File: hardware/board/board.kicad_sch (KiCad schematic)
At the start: 10 parts, among them J101 UART, J102 CM4_DEBUG, J103 DEBUG_PORT, U101 Oled

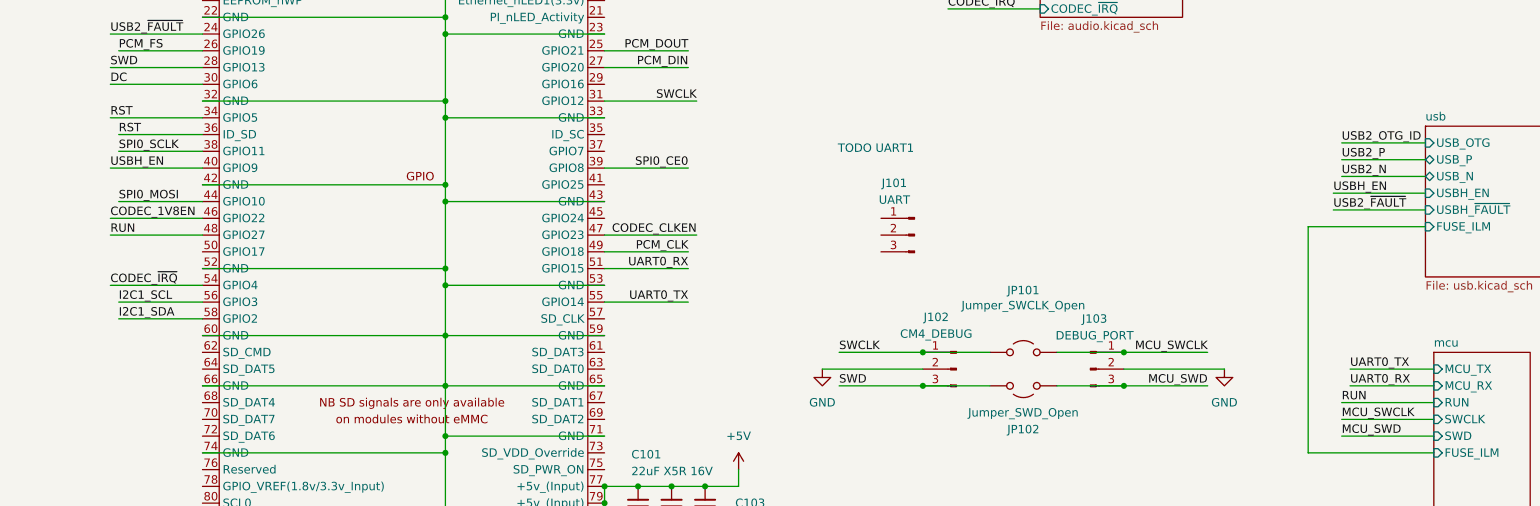
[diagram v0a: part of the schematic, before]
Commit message: wire encoder sw 3/4 and some cleanup
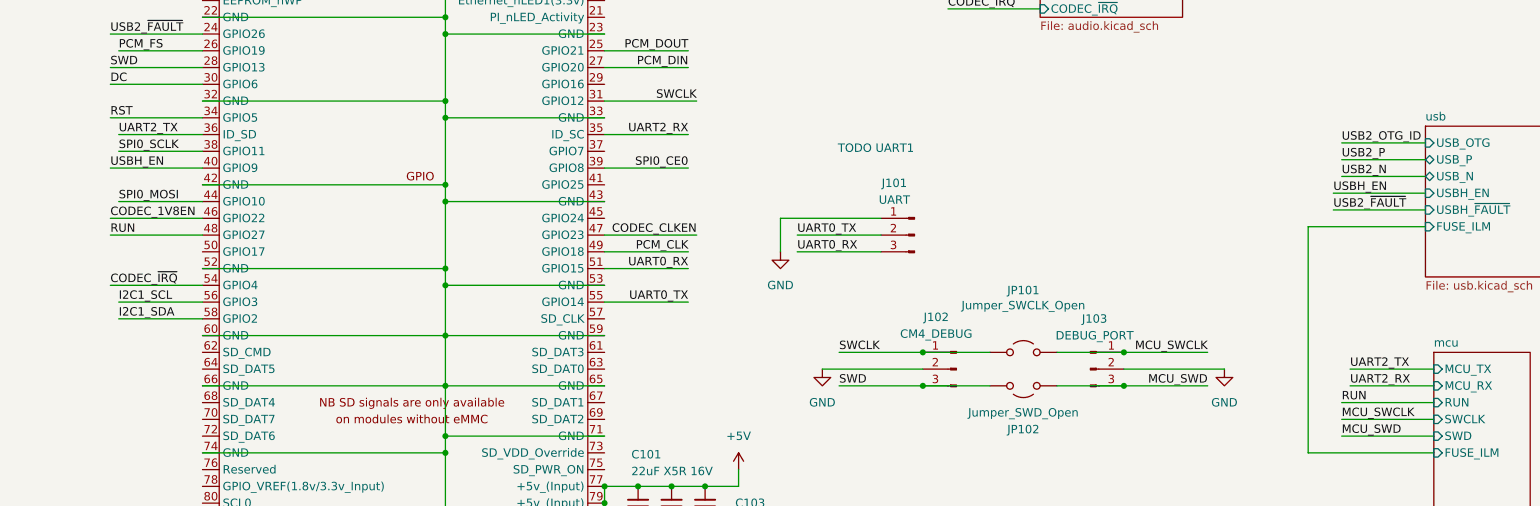
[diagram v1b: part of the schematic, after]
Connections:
- net GND: now also J101.1 (Pin_1)
- net RST: no longer Module101.36 (ID_SD)
- net UART0_RX: now also J101.3 (Pin_3)
- net UART0_TX: now also J101.2 (Pin_2)
- net UART2_RX: now reaches Module101.35 (ID_SC)
- new net UART2_TX: Module101.36 (ID_SD)
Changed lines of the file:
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@@
+	(wire
+		(pts
+			(xy 240.03 102.87) (xy 240.03 107.95)
+		)
+		(stroke
+			(width 0)
+			(type default)
+		)
+	)
 	(wire
 		(pts
@@
 	(wire
 		(pts
+			(xy 242.57 105.41) (xy 255.27 105.41)
+		)
+		(stroke
+			(width 0)
+			(type default)
+		)
+	)
+	(wire
+		(pts
 			(xy 261.62 128.27) (xy 271.78 128.27)
 		)
@@
 	(wire
 		(pts
+			(xy 242.57 107.95) (xy 255.27 107.95)
+		)
+		(stroke
+			(width 0)
+			(type default)
+		)
+	)
+	(wire
+		(pts
+			(xy 31.75 86.36) (xy 31.75 93.98)
+		)
+		(stroke
+			(width 0)
+			(type default)
+		)
+	)
+	(wire
+		(pts
+			(xy 138.43 74.93) (xy 152.4 74.93)
+		)
+		(stroke
+			(width 0)
+			(type default)
+		)
+	)
+	(wire
+		(pts
+			(xy 189.23 110.49) (xy 189.23 113.03)
+		)
+		(stroke
+			(width 0)
+			(type default)
+		)
+	)
+	(wire
+		(pts
+			(xy 255.27 102.87) (xy 240.03 102.87)
+		)
+		(stroke
+			(width 0)
+			(type default)
+		)
+	)
+	(wire
+		(pts
+			(xy 99.06 93.98) (xy 106.045 93.98)
+		)
+		(stroke
+			(width 0)
+			(type default)
+		)
+	)
+	(wire
+		(pts
+			(xy 189.23 54.61) (xy 189.23 62.23)
+		)
+		(stroke
+			(width 0)
+			(type default)
+		)
+	)
+	(wire
+		(pts
+			(xy 189.23 120.65) (xy 213.36 120.65)
+		)
+		(stroke
+			(width 0)
+			(type default)
+		)
+	)
+	(wire
+		(pts
+			(xy 31.75 139.7) (xy 31.75 147.32)
+		)
+		(stroke
+			(width 0)
+			(type default)
+		)
+	)
+	(wire
+		(pts
+			(xy 31.75 124.46) (xy 31.75 132.08)
+		)
+		(stroke
+			(width 0)
+			(type default)
+		)
+	)
+	(wire
+		(pts
+			(xy 106.045 78.74) (xy 106.045 86.36)
+		)
+		(stroke
+			(width 0)
+			(type default)
+		)
+	)
+	(wire
+		(pts
+			(xy 138.43 105.41) (xy 152.4 105.41)
+		)
+		(stroke
+			(width 0)
+			(type default)
+		)
+	)
+	(wire
+		(pts
 			(xy 326.39 125.73) (xy 339.09 125.73)
 		)
@@
 	(wire
 		(pts
-			(xy 31.75 86.36) (xy 31.75 93.98)
-		)
-		(stroke
-			(width 0)
-			(type default)
-		)
-	)
-	(wire
-		(pts
-			(xy 138.43 74.93) (xy 152.4 74.93)
-		)
-		(stroke
-			(width 0)
-			(type default)
-		)
-	)
-	(wire
-		(pts
-			(xy 189.23 110.49) (xy 189.23 113.03)
-		)
-		(stroke
-			(width 0)
-			(type default)
-		)
-	)
-	(wire
-		(pts
-			(xy 99.06 93.98) (xy 106.045 93.98)
-		)
-		(stroke
-			(width 0)
-			(type default)
-		)
-	)
-	(wire
-		(pts
-			(xy 189.23 54.61) (xy 189.23 62.23)
-		)
-		(stroke
-			(width 0)
-			(type default)
-		)
-	)
-	(wire
-		(pts
-			(xy 189.23 120.65) (xy 213.36 120.65)
-		)
-		(stroke
-			(width 0)
-			(type default)
-		)
-	)
-	(wire
-		(pts
-			(xy 31.75 139.7) (xy 31.75 147.32)
-		)
-		(stroke
-			(width 0)
-			(type default)
-		)
-	)
-	(wire
-		(pts
-			(xy 31.75 124.46) (xy 31.75 132.08)
-		)
-		(stroke
-			(width 0)
-			(type default)
-		)
-	)
-	(wire
-		(pts
-			(xy 106.045 78.74) (xy 106.045 86.36)
-		)
-		(stroke
-			(width 0)
-			(type default)
-		)
-	)
-	(wire
-		(pts
-			(xy 138.43 105.41) (xy 152.4 105.41)
-		)
-		(stroke
-			(width 0)
-			(type default)
-		)
-	)
-	(wire
-		(pts
 			(xy 189.23 120.65) (xy 189.23 128.27)
 		)
@@
 	(wire
 		(pts
+			(xy 226.06 90.17) (xy 213.36 90.17)
+		)
+		(stroke
+			(width 0)
+			(type default)
+		)
+	)
+	(wire
+		(pts
 			(xy 189.23 72.39) (xy 189.23 74.93)
 		)
@@
 	(wire
 		(pts
+			(xy 326.39 128.27) (xy 339.09 128.27)
+		)
+		(stroke
+			(width 0)
+			(type default)
+		)
+	)
+	(wire
+		(pts
 			(xy 106.045 71.12) (xy 106.045 78.74)
 		)
@@
 	(wire
 		(pts
-			(xy 326.39 128.27) (xy 339.09 128.27)
-		)
-		(stroke
-			(width 0)
-			(type default)
-		)
-	)
-	(wire
-		(pts
 			(xy 38.1 116.84) (xy 31.75 116.84)
 		)
@@
 			(width 0)
 			(type default)
+		)
+	)
+	(label "UART2_RX"
+		(at 226.06 90.17 180)
+		(effects
+			(font
+				(size 1.27 1.27)
+			)
+			(justify right bottom)
 		)
 	)
@@
 		)
 	)
-	(label "UART0_TX"
-		(at 326.39 125.73 0)
-		(effects
-			(font
-				(size 1.27 1.27)
-			)
-			(justify left bottom)
-		)
-	)
 	(label "SPI0_SCLK"
 		(at 139.7 92.71 0)
@@
 	)
 	(label "UART0_RX"
-		(at 326.39 128.27 0)
+		(at 242.57 107.95 0)
 		(effects
 			(font
@@
 		)
 	)
+	(label "UART0_TX"
+		(at 242.57 105.41 0)
+		(effects
+			(font
+				(size 1.27 1.27)
+			)
+			(justify left bottom)
+		)
+	)
 	(label "MCU_SWD"
 		(at 325.12 135.89 0)
@@
 		)
 	)
-	(label "RST"
+	(label "UART2_TX"
 		(at 139.7 90.17 0)
 		(effects
@@
 			)
 			(justify right bottom)
+		)
+	)
+	(label "UART2_TX"
+		(at 326.39 125.73 0)
+		(effects
+			(font
+				(size 1.27 1.27)
+			)
+			(justify left bottom)
+		)
+	)
+	(label "UART2_RX"
+		(at 326.39 128.27 0)
+		(effects
+			(font
+				(size 1.27 1.27)
+			)
+			(justify left bottom)
 		)
 	)
@@
 					(unit 1)
 				)
+			)
+		)
+	)
+	(symbol
+		(lib_id "power:GND")
+		(at 240.03 107.95 0)
+		(mirror y)
+		(unit 1)
+		(body_style 1)
+		(exclude_from_sim no)
+		(in_bom yes)
+		(on_board yes)
+		(in_pos_files yes)
+		(dnp no)
+		(fields_autoplaced yes)
+		(property "Reference" "#PWR0112"
+			(at 240.03 114.3 0)
+			(hide yes)
+			(show_name no)
+			(do_not_autoplace no)
+			(effects
+				(font
+					(size 1.27 1.27)
+				)
+			)
+		)
+		(property "Value" "GND"
+			(at 240.03 113.03 0)
+			(show_name no)
+			(do_not_autoplace no)
+			(effects
+				(font
+					(size 1.27 1.27)
+				)
+			)
+		)
+		(property "Footprint" ""
+			(at 240.03 107.95 0)
+			(hide yes)
+			(show_name no)
+			(do_not_autoplace no)
+			(effects
+				(font
+					(size 1.27 1.27)
+				)
+			)
+		)
+		(property "Datasheet" ""
+			(at 240.03 107.95 0)
+			(hide yes)
+			(show_name no)
+			(do_not_autoplace no)
+			(effects
+				(font
+					(size 1.27 1.27)
+				)
+			)
+		)
+		(property "Description" "Power symbol creates a global label with name \"GND\" , ground"
+			(at 240.03 107.95 0)
+			(hide yes)
+			(show_name no)
+			(do_not_autoplace no)
+			(effects
+				(font
+					(size 1.27 1.27)
+				)
+			)
+		)
+		(pin "1"
+		)
+		(instances
+			(project "board"
+				(path "/dd13fd41-39ab-4435-9074-5024f1786746"
+					(reference "#PWR0112")
+					(unit 1)
+				)

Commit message: idk
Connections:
- net USB2_~{FAULT}: now also Module101.80 (SCL0); no longer Module101.24 (GPIO26)
- net USBH_EN: now also Module101.82 (SDA0); no longer Module101.40 (GPIO9)
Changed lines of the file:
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@@
+	(wire
+		(pts
+			(xy 138.43 146.05) (xy 152.4 146.05)
+		)
+		(stroke
+			(width 0)
+			(type default)
+		)
+	)
 	(wire
 		(pts
@@
 	(wire
 		(pts
+			(xy 138.43 148.59) (xy 152.4 148.59)
+		)
+		(stroke
+			(width 0)
+			(type default)
+		)
+	)
+	(wire
+		(pts
 			(xy 189.23 168.91) (xy 189.23 177.8)
 		)
@@
 	(wire
 		(pts
-			(xy 138.43 74.93) (xy 152.4 74.93)
-		)
-		(stroke
-			(width 0)
-			(type default)
-		)
-	)
-	(wire
-		(pts
 			(xy 189.23 110.49) (xy 189.23 113.03)
 		)
@@
 		(pts
 			(xy 152.4 62.23) (xy 189.23 62.23)
-		)
-		(stroke
-			(width 0)
-			(type default)
-		)
-	)
-	(wire
-		(pts
-			(xy 138.43 95.25) (xy 152.4 95.25)
 		)
 		(stroke
@@
 		)
 	)
-	(label "USB2_~{FAULT}"
-		(at 138.43 74.93 0)
-		(effects
-			(font
-				(size 1.27 1.27)
-			)
-			(justify left bottom)
-		)
-	)
 	(label "CODEC_CLKEN"
 		(at 265.43 64.77 0)
@@
 		)
 	)
-	(label "USBH_EN"
-		(at 138.43 95.25 0)
-		(effects
-			(font
-				(size 1.27 1.27)
-			)
-			(justify left bottom)
-		)
-	)
 	(label "MCU_SWCLK"
 		(at 304.8 123.19 180)
@@
 		)
 	)
+	(label "USBH_EN"
+		(at 138.43 148.59 0)
+		(effects
+			(font
+				(size 1.27 1.27)
+			)
+			(justify left bottom)
+		)
+	)
 	(label "UART0_TX"
 		(at 242.57 105.41 0)
@@
 		(effects
 			(font
+				(size 1.27 1.27)
+			)
+			(justify left bottom)
+		)
+	)
+	(label "USB2_~{FAULT}"
+		(at 138.43 146.05 0)
+		(effects
+			(font

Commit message: fillout LCSC and swap micro usb
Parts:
- J101, J102, J103: LCSC (none) -> C52016391
- JP101, JP102, U101: now not fitted
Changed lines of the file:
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@@
+			)
+		)
+		(property "LCSC" "C52016391"
+			(at 260.35 105.41 0)
+			(hide yes)
+			(show_name no)
+			(do_not_autoplace no)
+			(effects
+				(font
+					(size 1.27 1.27)
+				)
 			)
 		)
@@
 		(on_board yes)
 		(in_pos_files yes)
-		(dnp no)
+		(dnp yes)
 		(property "Reference" "JP102"
 			(at 276.86 134.874 0)
@@
 		(on_board yes)
 		(in_pos_files yes)
-		(dnp no)
+		(dnp yes)
 		(property "Reference" "U101"
 			(at 270.002 166.37 0)
@@
 		(on_board yes)
 		(in_pos_files yes)
-		(dnp no)
+		(dnp yes)
 		(property "Reference" "JP101"
 			(at 276.86 113.792 0)
@@
 			)
 		)
+		(property "LCSC" "C52016391"
+			(at 266.7 125.73 0)
+			(hide yes)
+			(show_name no)
+			(do_not_autoplace no)
+			(effects
+				(font
+					(size 1.27 1.27)
+				)
+			)
+		)
 		(pin "2"
 		)
@@
 			(at 287.02 125.73 0)
 			(hide yes)
+			(show_name no)
+			(do_not_autoplace no)
+			(effects
+				(font
+					(size 1.27 1.27)
+				)
+			)
+		)
+		(property "LCSC" "C52016391"
+			(at 287.02 125.73 0)
+			(hide yes)

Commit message: finish LCSC
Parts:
- added U102, U103: (no value), Connector_Hirose_DF40:Hirose_DF40C-100DS-0.4V_2x50_P0.4mm, symbol util:hirose_dummy
- C101, C102, C103: LCSC (none) -> C90146
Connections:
- net +3V3: now also Module101.78 (GPIO_VREF(1.8v/3.3v_Input))
- net GND: no longer Module101.143 (HDMI1_HOTPLUG), Module101.149 (HDMI1_CEC)
- net SPI0_CE0: now also Module101.37 (GPIO7); no longer Module101.39 (GPIO8)
- net USB2_~{FAULT}: now also Module101.41 (GPIO25); no longer Module101.80 (SCL0)
- net USBH_EN: now also Module101.45 (GPIO24); no longer Module101.82 (SDA0)
- net UART4_RX: now reaches Module101.40 (GPIO9)
- net UART2_RX: no longer names the net of Module101.35 (ID_SC)
- net UART2_TX: no longer names the net of Module101.36 (ID_SD)
- new net UART4_TX: Module101.39 (GPIO8)

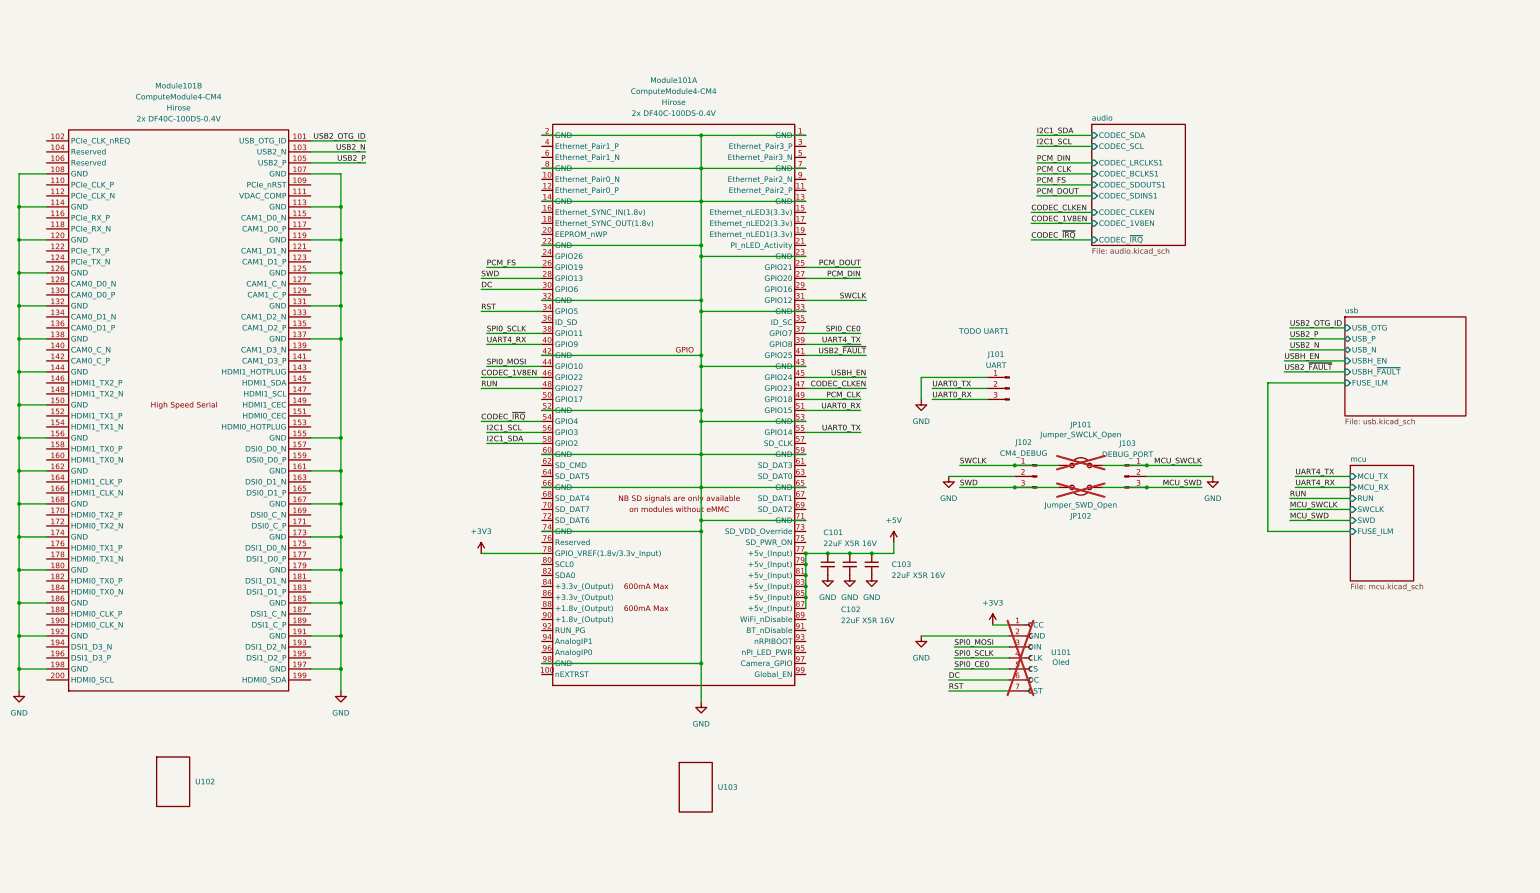
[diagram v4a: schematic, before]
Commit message: doublecheck cm4 mapping
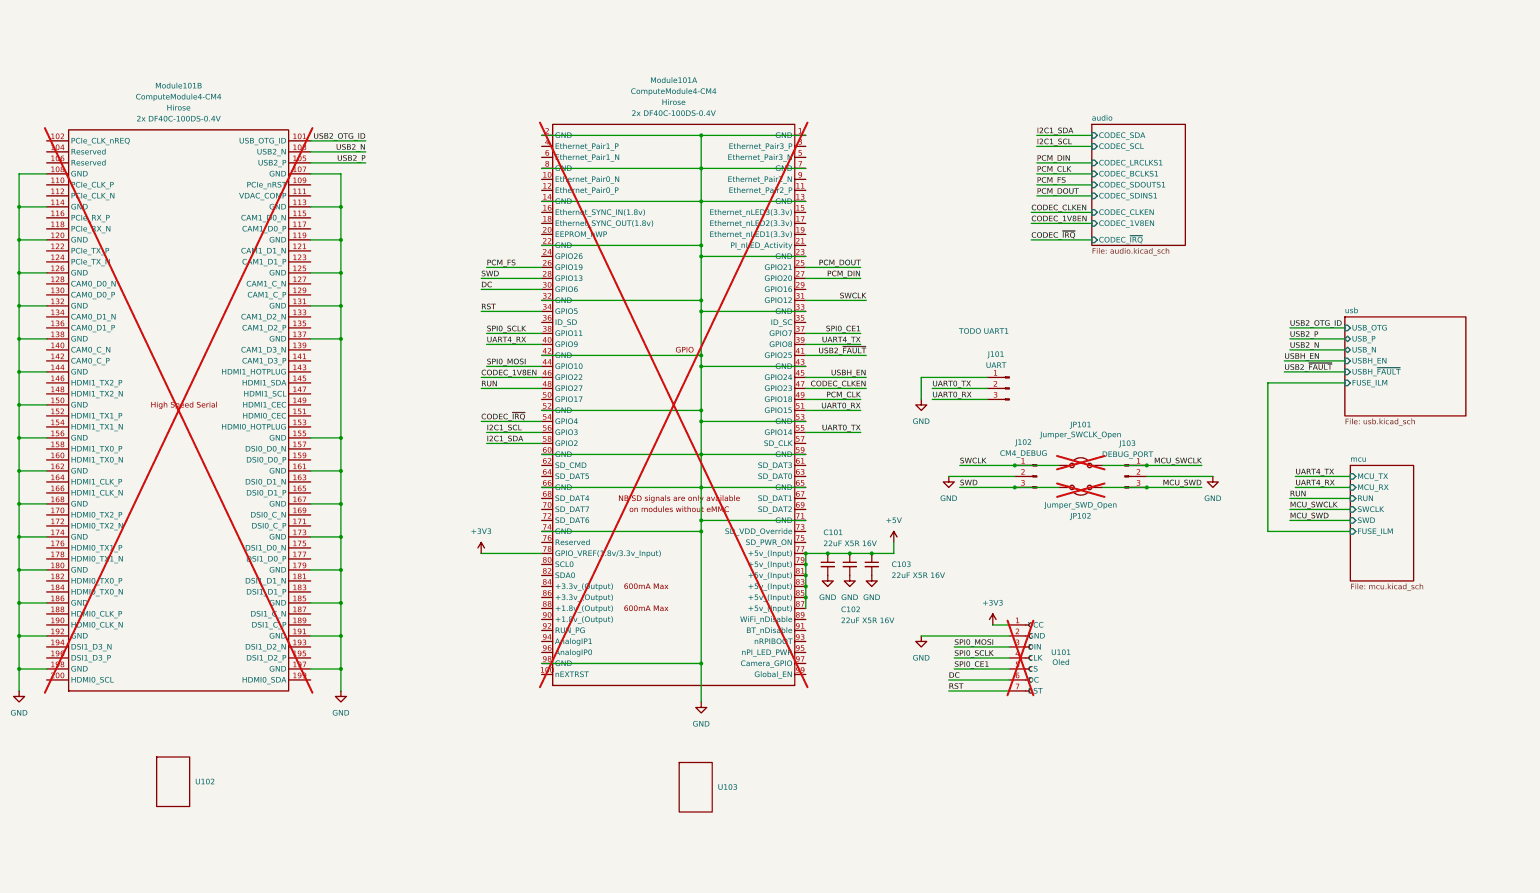
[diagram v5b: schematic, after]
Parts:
- Module101: now not fitted
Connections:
- net SPI0_CE0 renamed SPI0_CE1
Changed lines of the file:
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@@
 		)
 	)
-	(label "SPI0_CE0"
+	(label "SPI0_CE1"
 		(at 226.06 92.71 180)
 		(effects
@@
 		)
 	)
-	(label "SPI0_CE0"
+	(label "SPI0_CE1"
 		(at 247.65 170.18 0)
 		(effects
@@
 		(on_board yes)
 		(in_pos_files yes)
-		(dnp no)
+		(dnp yes)
 		(fields_autoplaced yes)
 		(property "Reference" "Module101"
@@
 		(on_board yes)
 		(in_pos_files yes)
-		(dnp no)
+		(dnp yes)
 		(fields_autoplaced yes)
 		(property "Reference" "Module101"

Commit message: use 2.54mm debug pins
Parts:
- J101, J102, J103: footprint Connector_PinHeader_1.27mm:PinHeader_1x03_P1.27mm_Vertical -> Connector_PinSocket_2.54mm:PinSocket_1x03_P2.54mm_Vertical
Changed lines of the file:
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@@
 			)
 		)
-		(property "Footprint" "Connector_PinHeader_1.27mm:PinHeader_1x03_P1.27mm_Vertical"
+		(property "Footprint" "Connector_PinSocket_2.54mm:PinSocket_1x03_P2.54mm_Vertical"
 			(at 260.35 105.41 0)
 			(hide yes)
@@
 			)
 		)
-		(property "Footprint" "Connector_PinHeader_1.27mm:PinHeader_1x03_P1.27mm_Vertical"
+		(property "Footprint" "Connector_PinSocket_2.54mm:PinSocket_1x03_P2.54mm_Vertical"
 			(at 266.7 125.73 0)
 			(hide yes)
@@
 			)
 		)
-		(property "Footprint" "Connector_PinHeader_1.27mm:PinHeader_1x03_P1.27mm_Vertical"
+		(property "Footprint" "Connector_PinSocket_2.54mm:PinSocket_1x03_P2.54mm_Vertical"
 			(at 287.02 125.73 0)
 			(hide yes)
